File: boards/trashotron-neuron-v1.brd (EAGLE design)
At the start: 88.9 x 50.8 mm, 28 parts, among them IC1 MCP604P, IC2 MCP604P, J6 455-1750-1-ND

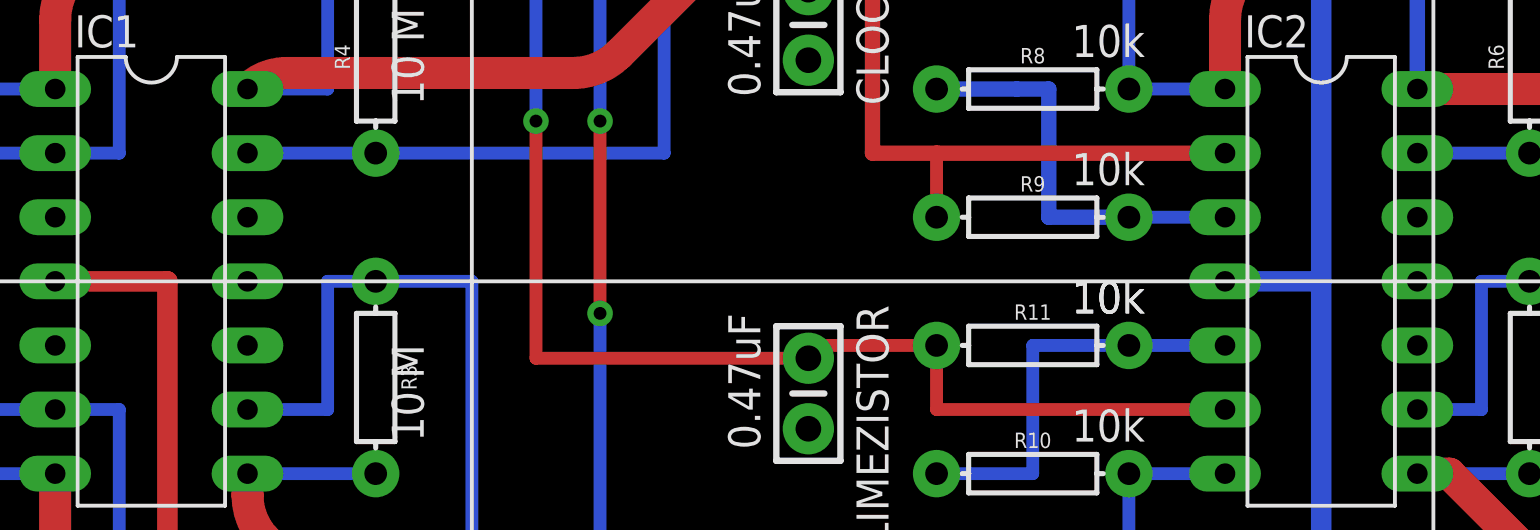
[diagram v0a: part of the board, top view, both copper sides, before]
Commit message: board development and  a longer default glyph
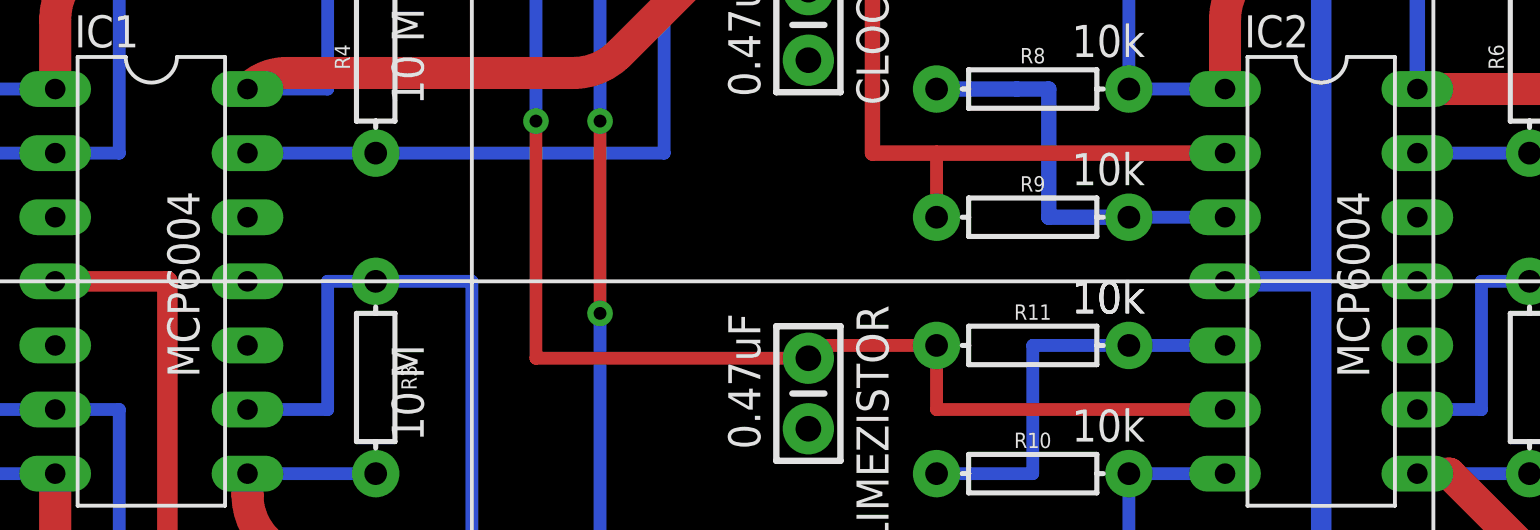
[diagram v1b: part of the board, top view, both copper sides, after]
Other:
- board text added: "MCP6004"
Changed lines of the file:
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@@
 <text x="23.495" y="46.99" size="1.27" layer="21" rot="R270">10uF</text>
 <text x="88.265" y="39.37" size="1.778" layer="21" rot="R180">5V</text>
+<text x="14.605" y="21.59" size="1.27" layer="21" rot="R90">MCP6004</text>
+<text x="60.96" y="21.59" size="1.27" layer="21" rot="R90">MCP6004</text>
 </plain>
 <attributes>
